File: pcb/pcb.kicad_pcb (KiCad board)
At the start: 2 copper layers, 81 x 80 mm, 1 part

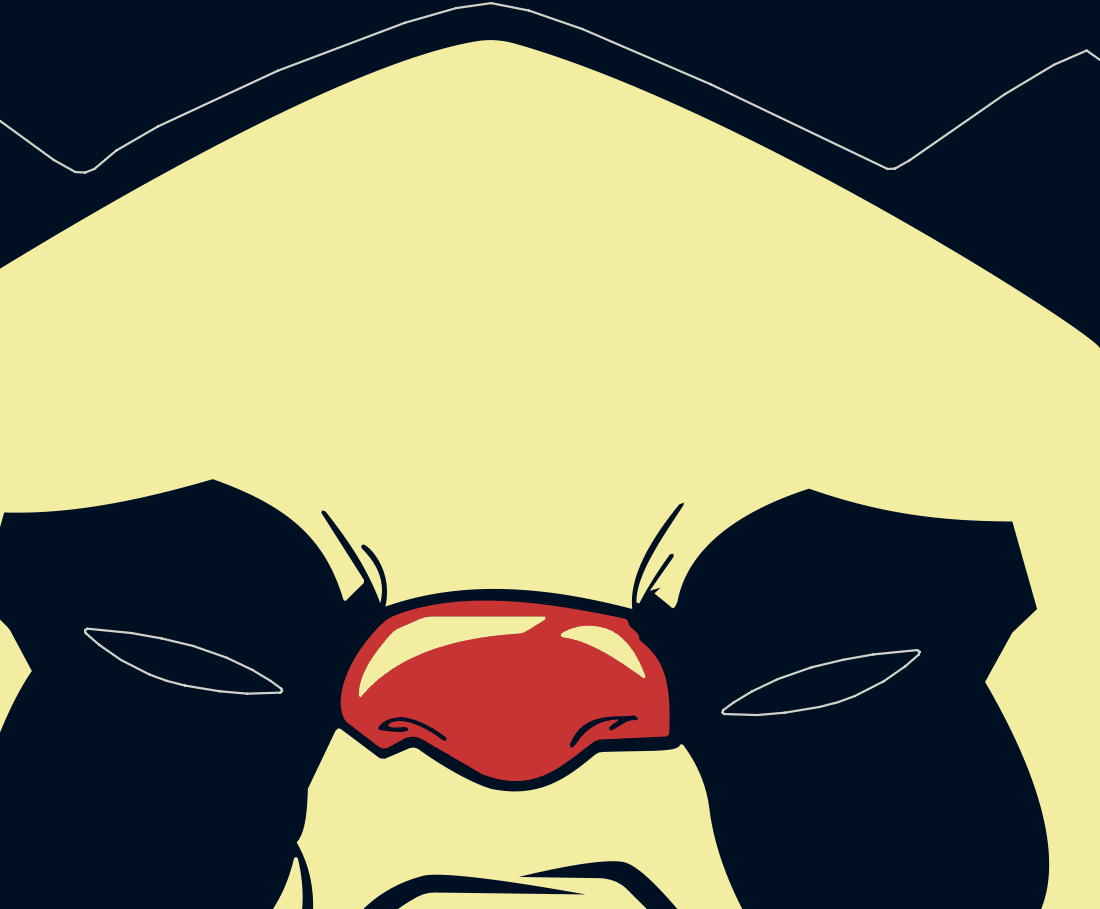
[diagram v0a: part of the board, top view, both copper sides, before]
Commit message: add leds + capacitive switch
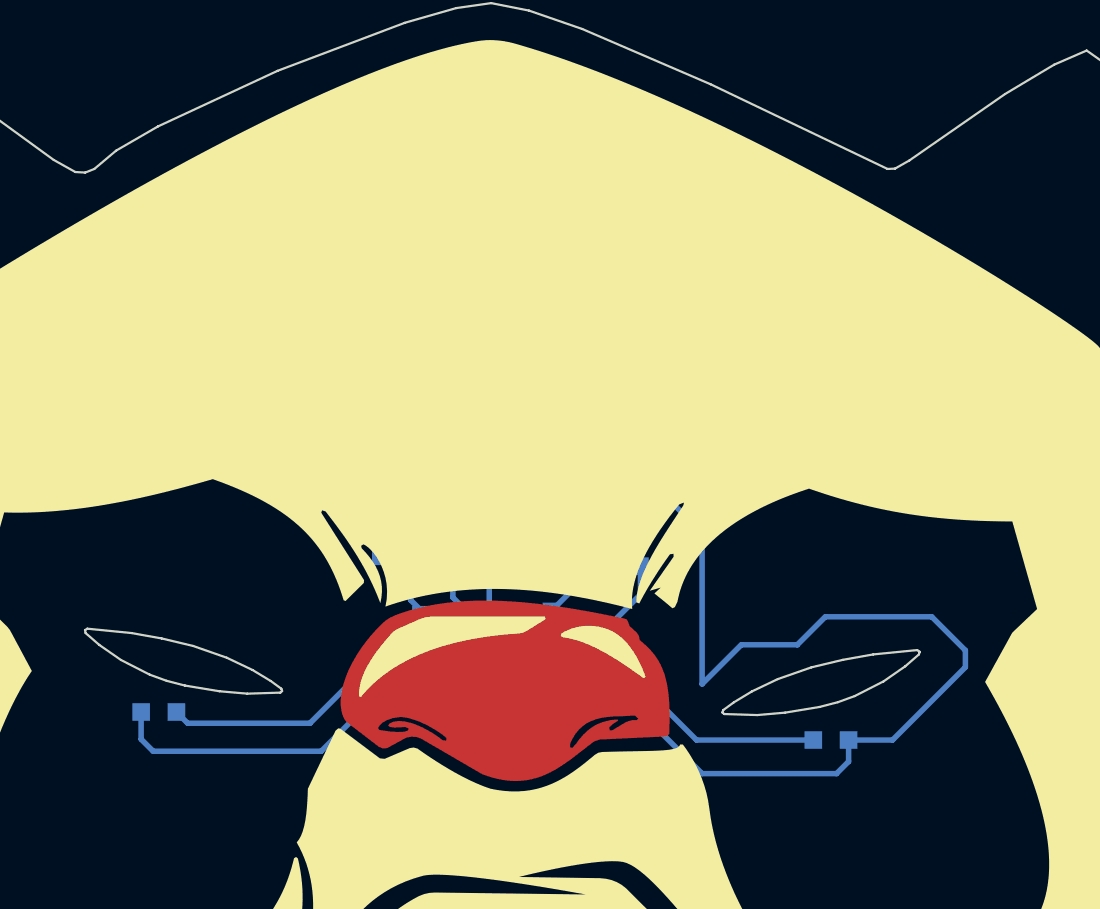
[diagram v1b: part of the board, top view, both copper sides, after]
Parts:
- added BT1: Battery_Cell, open-project:BAT_CR1216, B.Cu at (139.7, 50.8)
- added C1: 470nF, Capacitors_SMD:C_0603, B.Cu at (134.6, 59.7)
- added C2: 100nF, Capacitors_SMD:C_0603, B.Cu at (142.2, 66.0)
- added C3: 22pF, Capacitors_SMD:C_0603, B.Cu at (146.3, 62.5)
- added Cf1: C, Capacitors_SMD:C_0603, B.Cu at (138.4, 66.0)
- added D1: LED, LEDs:LED_0603, B.Cu at (154.9, 71.1)
- added D2: LED, LEDs:LED_0603, B.Cu at (124.5, 69.8)
- added Rc1: R, Resistors_SMD:R_0603, B.Cu at (136.4, 66.0)
- added Rf1: R, Resistors_SMD:R_0603, B.Cu at (135.1, 62.7)
- added U1: PCF8883, SMD_Packages:SOIC-8-N, B.Cu at (141.0, 61.0)
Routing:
- net LEDS: track 0.00 -> 71.3 mm
- net GND: track 0.00 -> 60.3 mm
- net VDD: track 0.00 -> 33.4 mm
- net Net-(Cf1-Pad1): track 0.00 -> 7.43 mm
- net Net-(C1-Pad1): track 0.00 -> 3.22 mm
- net Net-(C2-Pad1): track 0.00 -> 3.21 mm
- net Net-(C3-Pad2): track 0.00 -> 2.22 mm

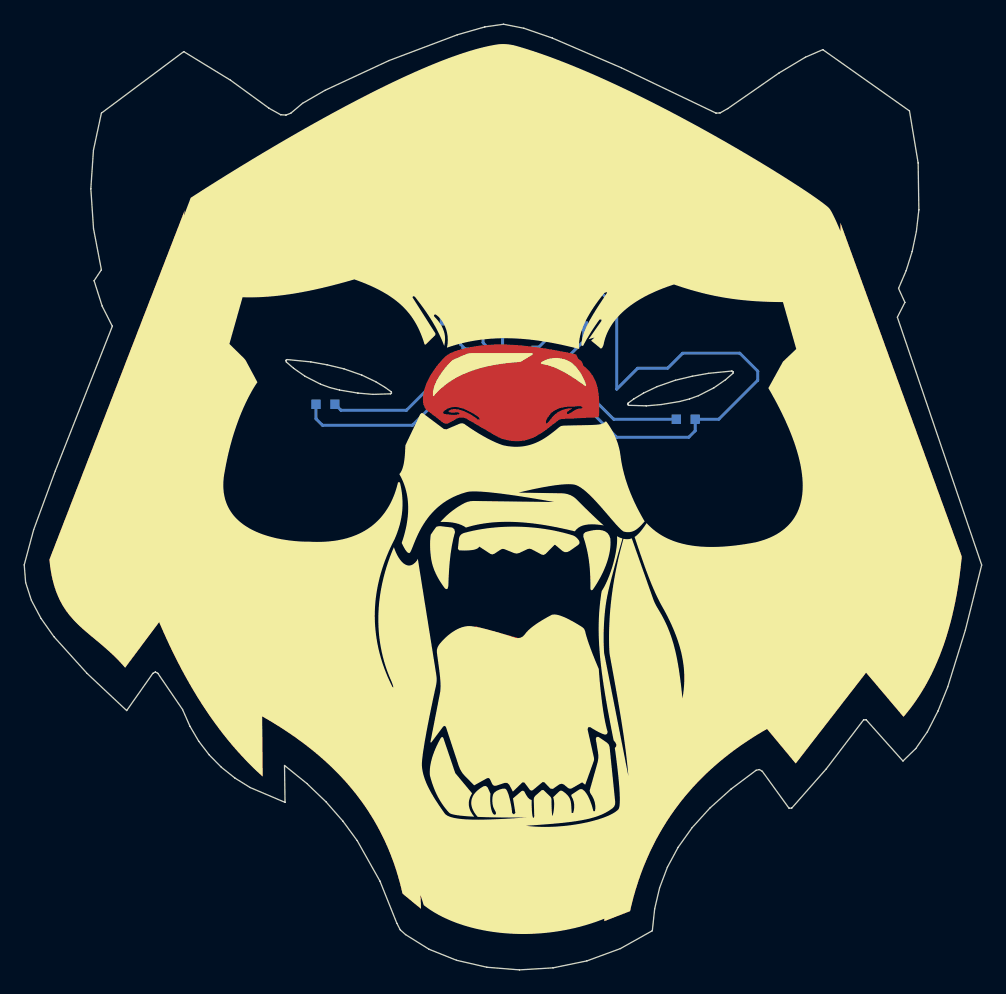
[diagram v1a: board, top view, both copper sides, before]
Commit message: add touch area, enlarge LEDs
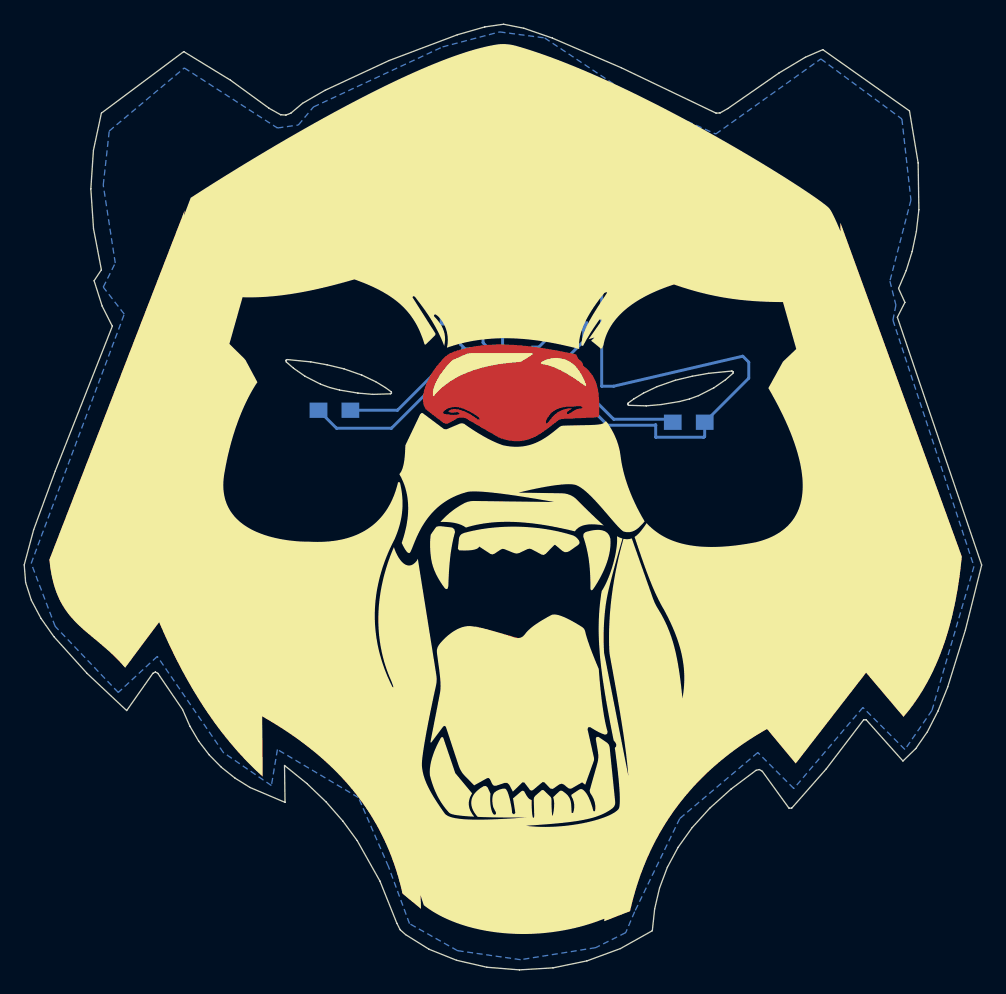
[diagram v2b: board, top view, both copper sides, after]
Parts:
- D1, D2: footprint LEDs:LED_0603 -> LEDs:LED_0805_HandSoldering
- moved D2 0.92 mm to (125.2, 70.4)
- moved D1 0.36 mm to (155.2, 71.4)
- renumbered Cf1 to Cf, Rc1 to Rc, Rf1 to Rf
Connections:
- net Net-(Rf1-Pad2) renamed TOUCH
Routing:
- net GND: track 60.3 -> 58.0 mm
- net LEDS: track 71.3 -> 70.0 mm
- added copper zone on B.Cu, net TOUCH

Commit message: fix unconnected pin
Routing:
- net GND: track 58.0 -> 59.7 mm
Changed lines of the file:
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@@
   (general
     (links 19)
-    (no_connects 1)
+    (no_connects 0)
     (area 98.929348 37.654584 180.026456 117.75246)
     (thickness 1.6)
     (drawings 142)
-    (tracks 59)
+    (tracks 61)
     (zones 0)
     (modules 11)
@@
     (35 F.Paste user hide)
     (36 B.SilkS user)
-    (37 F.SilkS user hide)
+    (37 F.SilkS user)
     (38 B.Mask user)
-    (39 F.Mask user hide)
+    (39 F.Mask user)
     (40 Dwgs.User user)
     (41 Cmts.User user)
@@
   (segment (start 147.35048 50.89906) (end 147.35048 55.84952) (width 0.25) (layer B.Cu) (net 1))
   (segment (start 147.35048 55.84952) (end 144.145 59.055) (width 0.25) (layer B.Cu) (net 1))
+  (segment (start 137.795 61.595) (end 139.446 61.595) (width 0.25) (layer B.Cu) (net 2))
   (segment (start 136.398 66.79) (end 134.124 66.79) (width 0.25) (layer B.Cu) (net 2))
   (segment (start 130.556 70.358) (end 126.572 70.358) (width 0.25) (layer B.Cu) (net 2))
@@
   (segment (start 145.796 68.072) (end 145.796 66.802) (width 0.25) (layer B.Cu) (net 2))
   (segment (start 148.844 71.12) (end 145.796 68.072) (width 0.25) (layer B.Cu) (net 2))
-  (segment (start 139.446 57.404) (end 139.446 66.04) (width 0.25) (layer B.Cu) (net 2))
+  (segment (start 139.446 57.404) (end 139.446 61.595) (width 0.25) (layer B.Cu) (net 2))
+  (segment (start 139.446 61.595) (end 139.446 66.04) (width 0.25) (layer B.Cu) (net 2))
   (segment (start 139.446 66.04) (end 140.196 66.79) (width 0.25) (layer B.Cu) (net 2))
   (segment (start 138.43 66.79) (end 136.398 66.79) (width 0.25) (layer B.Cu) (net 2))
